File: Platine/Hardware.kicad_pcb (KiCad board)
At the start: 2 copper layers, 245 x 250 mm, 151 parts, among them J1 Barrel_Jack, J2 Screw_Terminal_01x02, J3 USB_B, SW1 SW_Soft_Reset, SW2 SW_Hard_Reset, SW3 SW_Flash, U1 ESP32-WROOM-32D, U2 ZLDO1117_SOT223, U3 TS2596S, U4 FT232RL

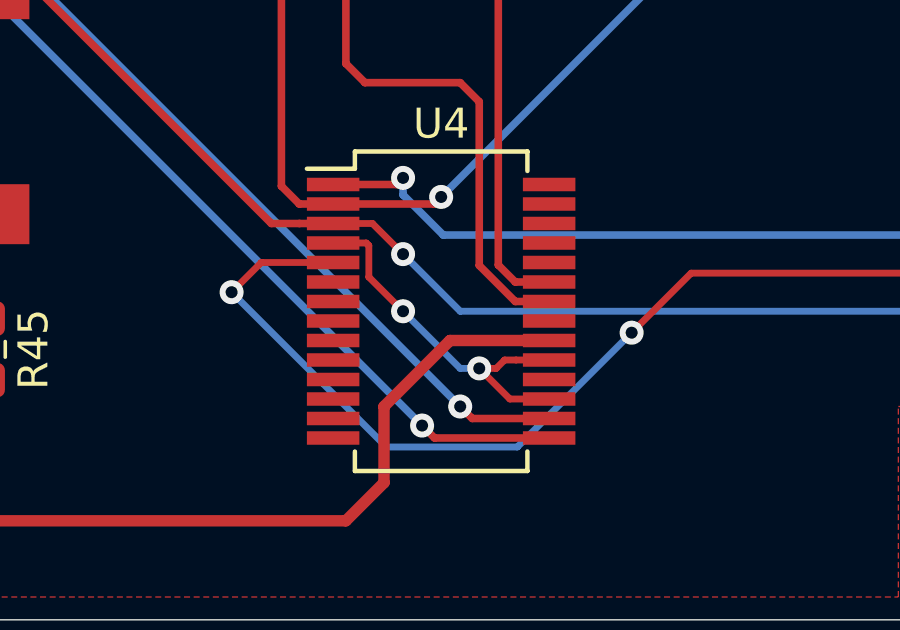
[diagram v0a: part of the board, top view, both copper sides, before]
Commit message: Updated Schematic to be more intuitive to read Updated BOM
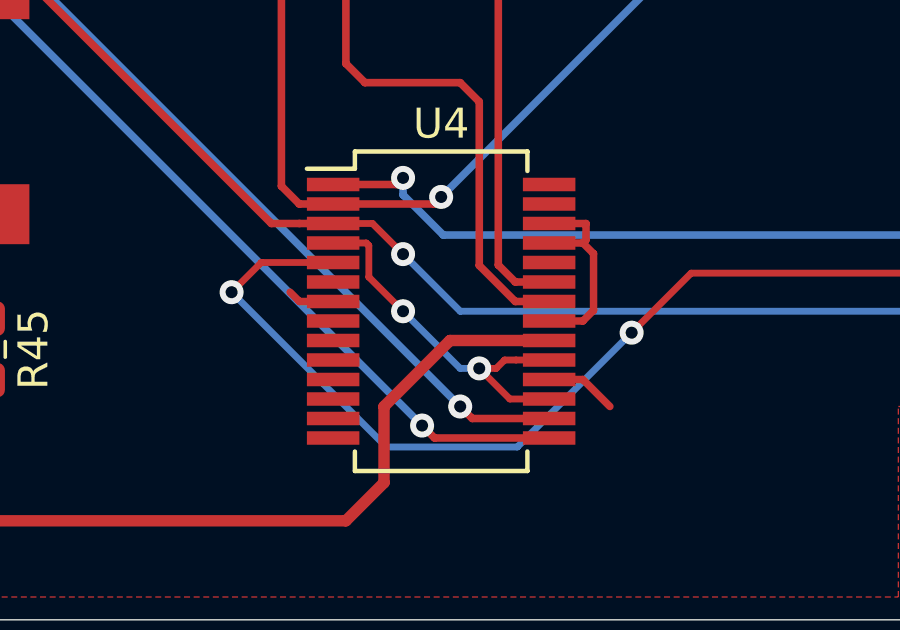
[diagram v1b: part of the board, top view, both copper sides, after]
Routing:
- net GND: track 0.00 -> 11.0 mm
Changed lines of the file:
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@@
-(kicad_pcb (version 20171130) (host pcbnew "(5.1.4)-1")
+(kicad_pcb (version 20171130) (host pcbnew "(5.1.5)-3")
   (general
     (thickness 1.6)
     (drawings 9)
-    (tracks 237)
+    (tracks 249)
     (zones 0)
     (modules 151)
@@
   )
   (setup
-    (last_trace_width 0.635)
+    (last_trace_width 0.25)
     (user_trace_width 0.2286)
     (user_trace_width 0.254)
@@
   (gr_line (start 265 20) (end 265 270) (layer Edge.Cuts) (width 0.05))
   (gr_line (start 20 20) (end 265 20) (layer Edge.Cuts) (width 0.05))
+  (segment (start 115.215 261.99) (end 116.115 262.89) (width 0.25) (layer F.Cu) (net 1))
+  (segment (start 114.09 261.99) (end 115.215 261.99) (width 0.25) (layer F.Cu) (net 1))
+  (segment (start 105.765 259.39) (end 105.455 259.08) (width 0.25) (layer F.Cu) (net 1))
+  (segment (start 106.89 259.39) (end 105.765 259.39) (width 0.25) (layer F.Cu) (net 1))
+  (segment (start 114.09 256.79) (end 115.32 256.79) (width 0.25) (layer F.Cu) (net 1))
+  (segment (start 115.32 257.335) (end 115.215 257.44) (width 0.25) (layer F.Cu) (net 1))
+  (segment (start 115.215 257.44) (end 114.09 257.44) (width 0.25) (layer F.Cu) (net 1))
+  (segment (start 115.32 256.79) (end 115.32 257.335) (width 0.25) (layer F.Cu) (net 1))
+  (segment (start 115.215 260.04) (end 115.57 259.685) (width 0.25) (layer F.Cu) (net 1))
+  (segment (start 114.09 260.04) (end 115.215 260.04) (width 0.25) (layer F.Cu) (net 1))
+  (segment (start 115.57 257.795) (end 115.215 257.44) (width 0.25) (layer F.Cu) (net 1))
+  (segment (start 115.57 259.685) (end 115.57 257.795) (width 0.25) (layer F.Cu) (net 1))
   (segment (start 212.09 235.745) (end 211.93 235.585) (width 0.762) (layer F.Cu) (net 2))
   (segment (start 212.09 243.3125) (end 212.09 235.745) (width 0.762) (layer F.Cu) (net 2))

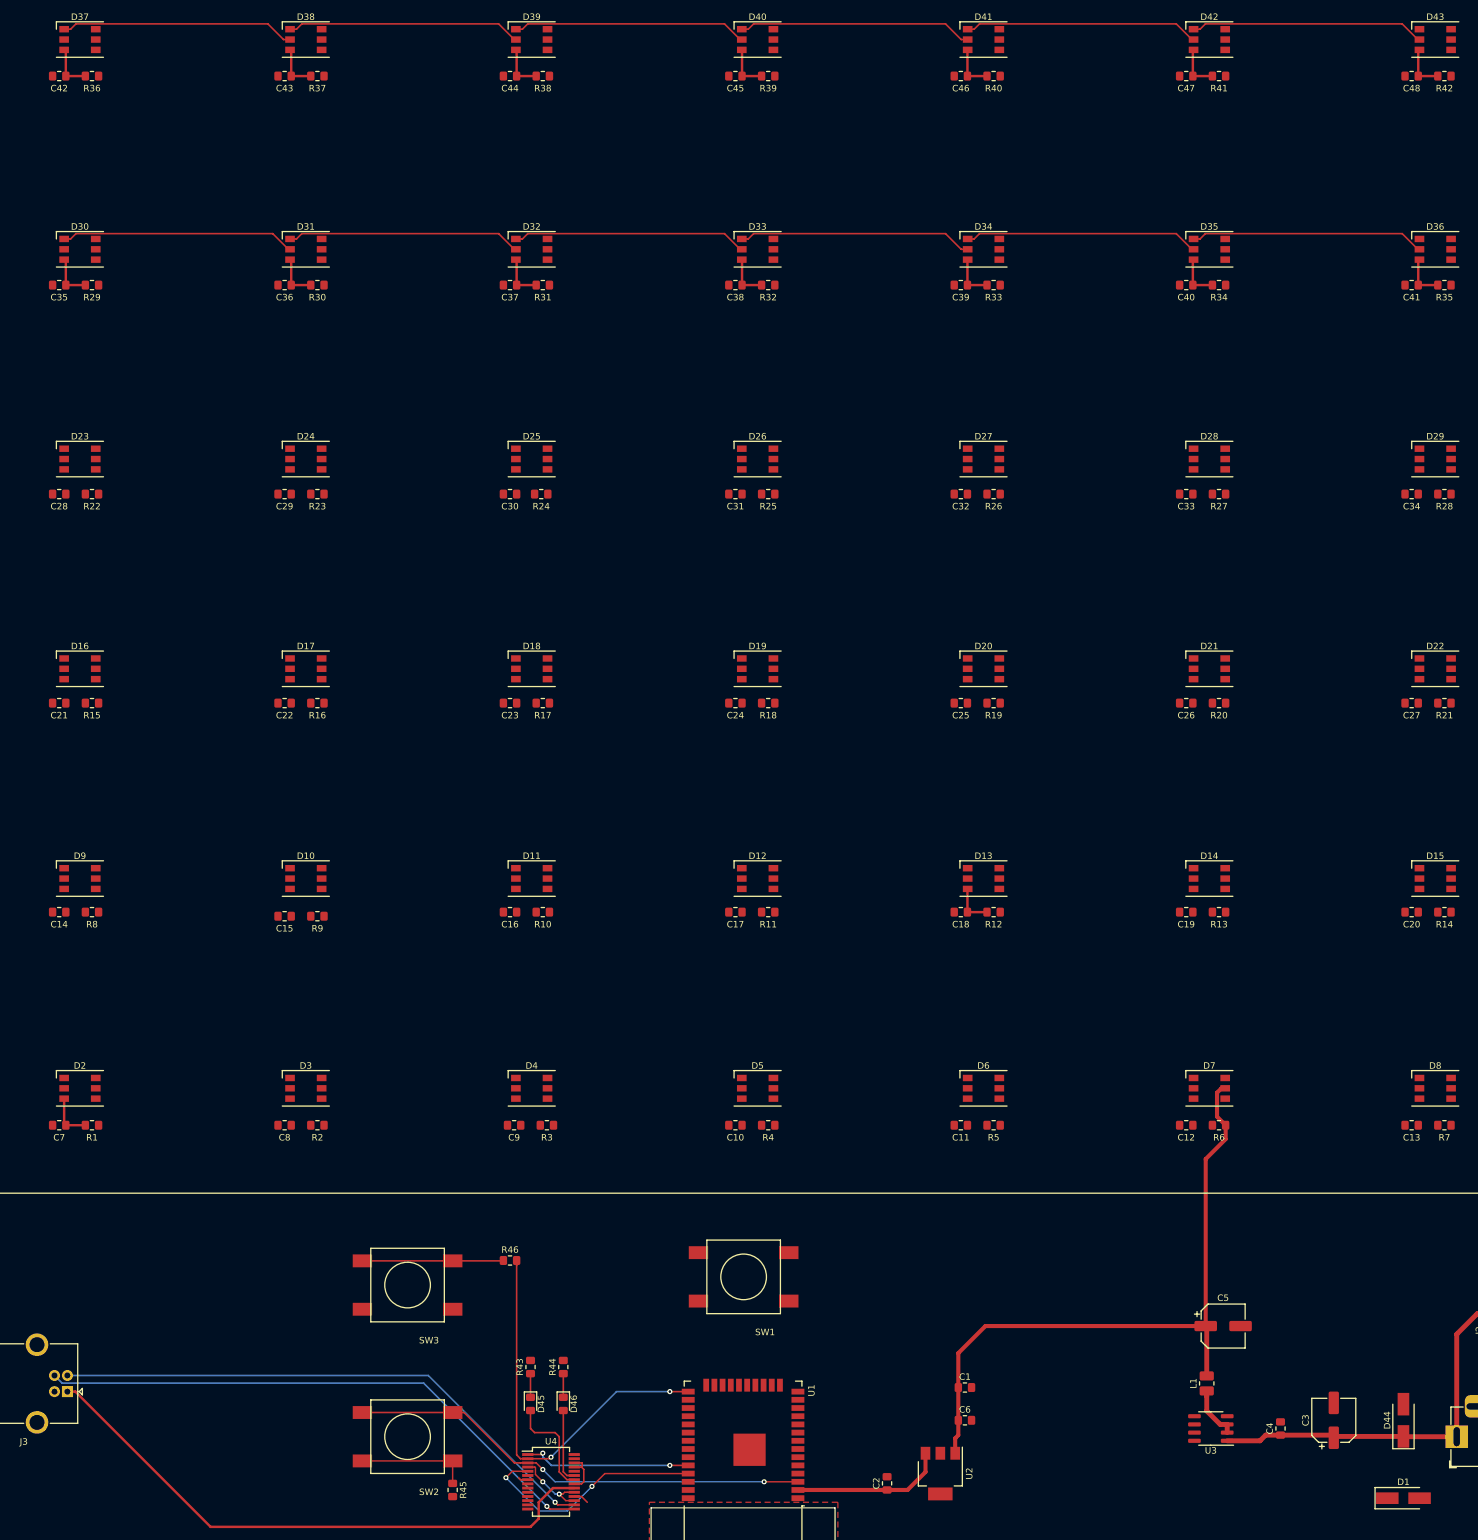
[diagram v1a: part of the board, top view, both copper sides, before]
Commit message: Added Enclosure plan
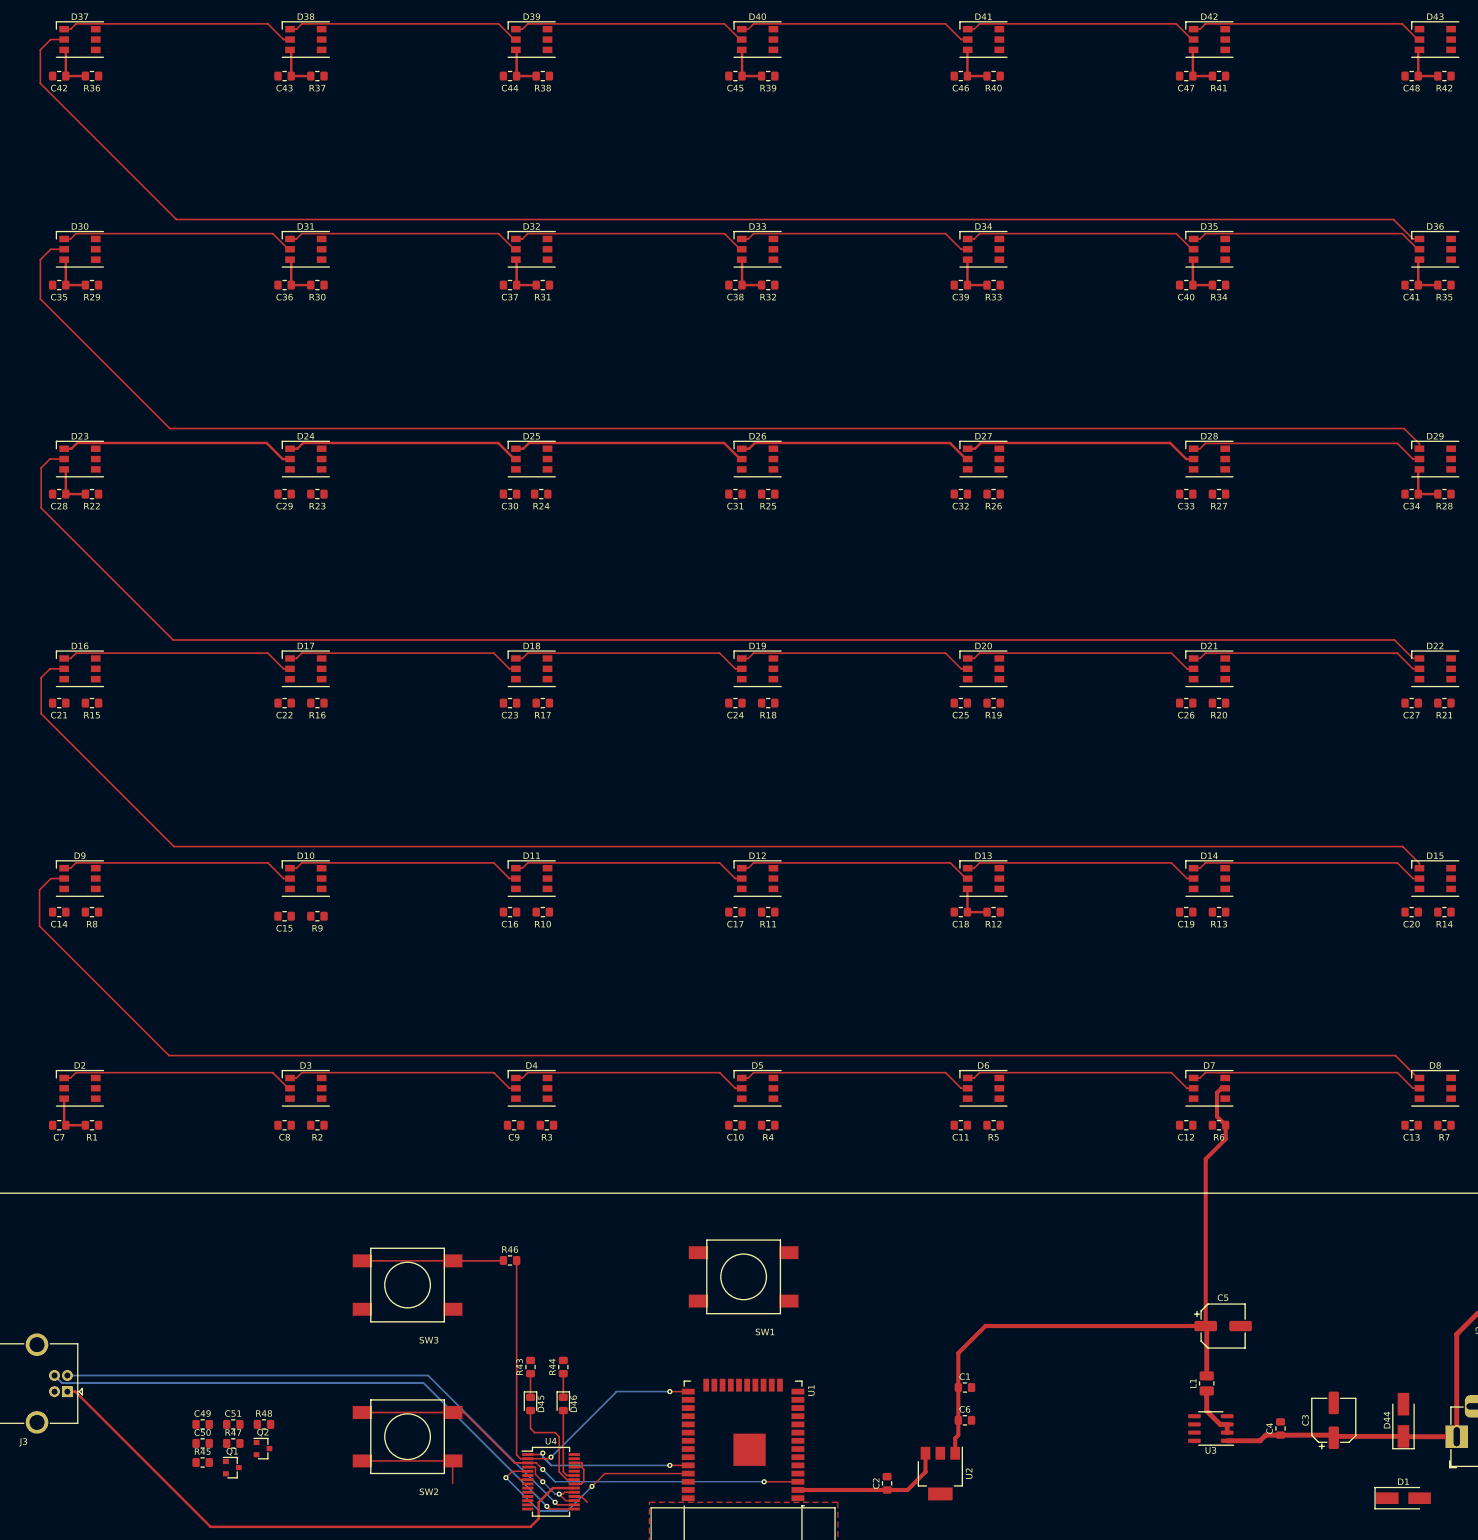
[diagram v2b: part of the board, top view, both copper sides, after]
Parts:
- added C49: 100n, Capacitor_SMD:C_0805_2012Metric_Pad1.15x1.40mm_HandSolder, F.Cu at (56.5, 250.8)
- added C50: 100n, Capacitor_SMD:C_0805_2012Metric_Pad1.15x1.40mm_HandSolder, F.Cu at (56.5, 253.8)
- added C51: 4.7u, Capacitor_SMD:C_0805_2012Metric_Pad1.15x1.40mm_HandSolder, F.Cu at (61.3, 250.8)
- added Q1: BCX19, Package_TO_SOT_SMD:SOT-23, F.Cu at (61.1, 257.5)
- added Q2: BCX19, Package_TO_SOT_SMD:SOT-23, F.Cu at (65.9, 254.6)
- added R47: 10k, Resistor_SMD:R_0805_2012Metric_Pad1.15x1.40mm_HandSolder, F.Cu at (61.3, 253.8)
- added R48: 10k, Resistor_SMD:R_0805_2012Metric_Pad1.15x1.40mm_HandSolder, F.Cu at (66.0, 250.8)
- R45: value 470 -> 10k
- moved R45 39.0 mm to (56.5, 256.7), turned to 0 degrees
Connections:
- net Net-(D2-Pad2) renamed LED_DATA
- net Net-(J3-Pad1) renamed V_USB
- net Net-(U4-Pad17) renamed V_FT_IO
- R45 pad 1: Net-(R45-Pad1) -> VCCQ
- R45 pad 2: GND -> ESP_ENA
- R46 pad 1: Net-(R46-Pad1) -> VCCQ
- R46 pad 2: Net-(R46-Pad2) -> GPIO_0
- SW1 pad 1: Net-(SW1-Pad1) -> GND
- SW1 pad 2: GND -> IO_S_RST
- SW2 pad 1: Net-(R45-Pad1) -> GND
- SW2 pad 2: Net-(SW2-Pad2) -> ESP_ENA
- SW3 pad 2: Net-(R46-Pad1) -> GPIO_0
- U1 pad 25: Net-(R46-Pad2) -> GPIO_0
- U1 pad 3: Net-(SW2-Pad2) -> ESP_ENA
- U1 pad 34: Net-(U1-Pad34) -> TX0
- U1 pad 35: Net-(U1-Pad35) -> RX0
- U1 pad 7: Net-(SW1-Pad1) -> IO_S_RST
- U4 pad 1: Net-(U1-Pad34) -> RX0
- U4 pad 2: Net-(R46-Pad2) -> DTR
- U4 pad 3: Net-(SW2-Pad2) -> RTS
- U4 pad 5: Net-(U1-Pad35) -> TX0
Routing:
- net Net-(D29-Pad1): track 0.00 -> 234.2 mm
- net Net-(D8-Pad1): track 0.00 -> 233.7 mm
- net Net-(D15-Pad1): track 0.00 -> 233.6 mm
- net Net-(D22-Pad1): track 0.00 -> 233.6 mm
- net Net-(D36-Pad1): track 0.00 -> 233.2 mm
- net Net-(D25-Pad1): track 0.00 -> 36.4 mm
- net Net-(D24-Pad1): track 0.00 -> 36.4 mm
- net Net-(D23-Pad1): track 0.00 -> 36.4 mm
- net Net-(D27-Pad1): track 0.00 -> 36.4 mm
- net Net-(D26-Pad1): track 0.00 -> 36.4 mm
- net Net-(D28-Pad1): track 0.00 -> 36.3 mm
- net Net-(D4-Pad1): track 0.00 -> 36.3 mm
- net Net-(D18-Pad1): track 0.00 -> 36.3 mm
- net Net-(D11-Pad1): track 0.00 -> 36.3 mm
- net Net-(D7-Pad1): track 0.00 -> 36.3 mm
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
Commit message: Finished PCB Layout V1 Updated Inductor for ripple reduction Rerouted FT232RL traces Added reset logic for ISP programming Added Silkscreen button labels
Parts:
- L1: footprint Custom_Footprints:L_1008_2520Metric_Pad1.43x2.20mm_HandSolder -> Inductor_SMD:L_10.4x10.4_H4.8
- moved R45 102.5 mm to (159.0, 260.0), turned to 90 degrees
- moved R46 70.8 mm to (166.0, 260.0), turned to 90 degrees
- moved R48 50.2 mm to (114.3, 264.7), turned to 270 degrees
- moved Q2 49.6 mm to (115.2, 260.1), turned to 90 degrees
- moved R47 48.3 mm to (108.3, 264.7), turned to 270 degrees
- moved C49 48.3 mm to (104.8, 251.3), turned to 270 degrees
- moved Q1 48.2 mm to (109.2, 260.1), turned to 90 degrees
- moved C50 45.5 mm to (101.2, 245.4), turned to 90 degrees
- moved C51 40.0 mm to (101.2, 251.3), turned to 270 degrees
- moved D1 33.4 mm to (214.6, 244.0)
- moved U2 31.6 mm to (201.7, 251.5), turned to 0 degrees
- moved C6 25.0 mm to (197.5, 240.2), turned to 180 degrees
- moved C1 22.9 mm to (197.5, 243.7), turned to 180 degrees
- moved C5 12.8 mm to (214.8, 222.8)
- moved L1 10.2 mm to (212.1, 234.3)
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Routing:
- net VCC: track 103.1 -> 265.4 mm, vias 0 -> 93
- net LED_DATA: track 0.00 -> 147.3 mm, vias 0 -> 2
- net GPIO_0: track 0.00 -> 130.0 mm, vias 0 -> 4
- net ESP_ENA: track 0.00 -> 86.4 mm, vias 0 -> 2
- net Net-(SW2-Pad2): track 71.9 -> 0.00 mm, vias 2 -> 0
- net Net-(R46-Pad2): track 61.3 -> 0.00 mm, vias 2 -> 0
- net IO_S_RST: track 0.00 -> 43.0 mm
- net Net-(U1-Pad35): track 36.6 -> 0.00 mm, vias 2 -> 0
- net VCCQ: track 23.8 -> 54.0 mm
- net Net-(U1-Pad34): track 26.1 -> 0.00 mm, vias 2 -> 0
- net Net-(R46-Pad1): track 21.9 -> 0.00 mm
- net RTS: track 0.00 -> 18.5 mm
- net DTR: track 0.00 -> 17.8 mm, vias 0 -> 2
- net TX0: track 0.00 -> 17.8 mm
- net RX0: track 0.00 -> 17.3 mm
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- added copper zone on B.Cu, net GND
- added copper zone on B.Cu, net VCC
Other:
- board text added: "Boot Mode"
- board text added: "Hard Reset"
- board text added: "Soft Reset"
- board text added: "V input: 6 - 28 V A max: 2 A"

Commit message: Finished review of Layout Reviewed BOM Added input cutoff form screw terminal when barreljack is used Added branding Added revision Added author Optimised routing Added screw holes for case Updated barreljack footprint
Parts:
- added G***: Sees_LOGO, Custom_Footprints:Sees_Logo, F.Cu at (55.5, 257.0)
- added TP1: TestPoint 3V3, TestPoint:TestPoint_Pad_D2.0mm, F.Cu at (170.0, 261.0)
- added TP2: TestPoint 5V, TestPoint:TestPoint_Pad_D2.0mm, F.Cu at (198.5, 232.5)
- added TP3: TestPoint Vin, TestPoint:TestPoint_Pad_D2.0mm, F.Cu at (219.5, 253.5)
- added TP4: TestPoint Vusb, TestPoint:TestPoint_Pad_D2.0mm, F.Cu at (44.0, 246.5)
- added TP5: TestPoint Vftio, TestPoint:TestPoint_Pad_D2.0mm, F.Cu at (104.5, 239.5)
- D44: value D -> B340A
- J1: value Barrel_Jack -> Barrel_Jack_Switch; footprint Connector_BarrelJack:BarrelJack_Horizontal -> Custom_Footprints:BarrelJack_BKL_072759
- R43, R44: value 220 -> 300
- moved C50 2.29 mm to (103.5, 245.5), turned to 180 degrees
- moved J1 0.64 mm to (251.5, 252.7), turned to 90 degrees
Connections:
- J1 pad 3: (no net) -> Net-(J1-Pad3)
- J2 pad 1: GND -> Net-(C3-Pad1)
- J2 pad 2: Net-(C3-Pad1) -> Net-(J1-Pad3)
- R43 pad 2: GND -> V_FT_IO
- R44 pad 2: GND -> V_FT_IO
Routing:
- net V_FT_IO: track 20.4 -> 36.9 mm
- net Net-(J1-Pad3): track 0.00 -> 16.4 mm
- net Net-(C3-Pad1): track 62.7 -> 64.5 mm
- net V_USB: track 75.8 -> 76.9 mm
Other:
- outline, holes or cut-outs redrawn
- board text added: "Designed by Linda Heinrich & Mathis Lehmann Version 1.0 PSP2020 © Siemens Mobility GmbH"
- board text added: "StiP19"
